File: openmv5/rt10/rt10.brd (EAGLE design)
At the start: 35.6 x 44.5 mm, 220 parts, among them CN1 S2B-PH-K-S(LF)(SN), IC1 LM66200DRLR, IC2 AP61300Z6-7, IC3 IS42S16160G-6BL, IC4 ATECC608B-MAHDA-T, IC5 IS25LP064D-JKLE-TR, IC6 IS25LP128F-JKLE-TR, IC7 MXC4005XC, IC8 MIMXRT1052DVL6B, IC9 KSZ8081RNDCA-TR, J1 USB4105-GF-A, J2 DNP, J3 DNP, J4 DF12-36-DS, J5 USD-1040310811, J6 DNP, J7 DNP, J8 3221-10-0300-00, M1 9774030151R, M2 9774030151R, Q1 2N7002KW_R1_00001, Q2 2N7002KW_R1_00001, Q3 2N7002KW_R1_00001, Q4 2N7002KW_R1_00001, Q5 2N7002KW_R1_00001, U1 MIC5365-3.3YMT-TZ, U2 BQ24075RGTR, U3 LBEE5KL1DX-883, Y1 SC32S-7PF20PPM, Y2 XRCGB24M000F3M00R0

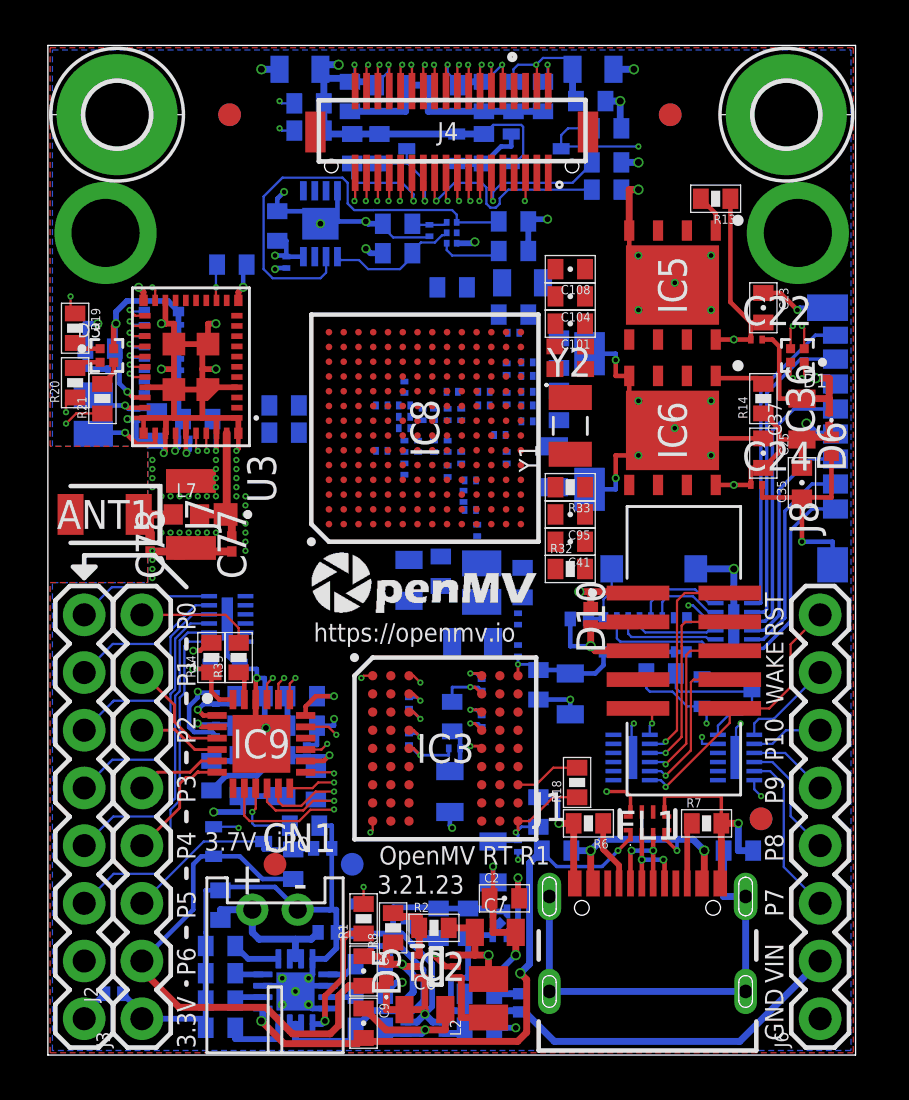
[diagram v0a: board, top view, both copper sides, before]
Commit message: Fix reverse protection on VIN, add TVS on FSIN, and fix USB current limits
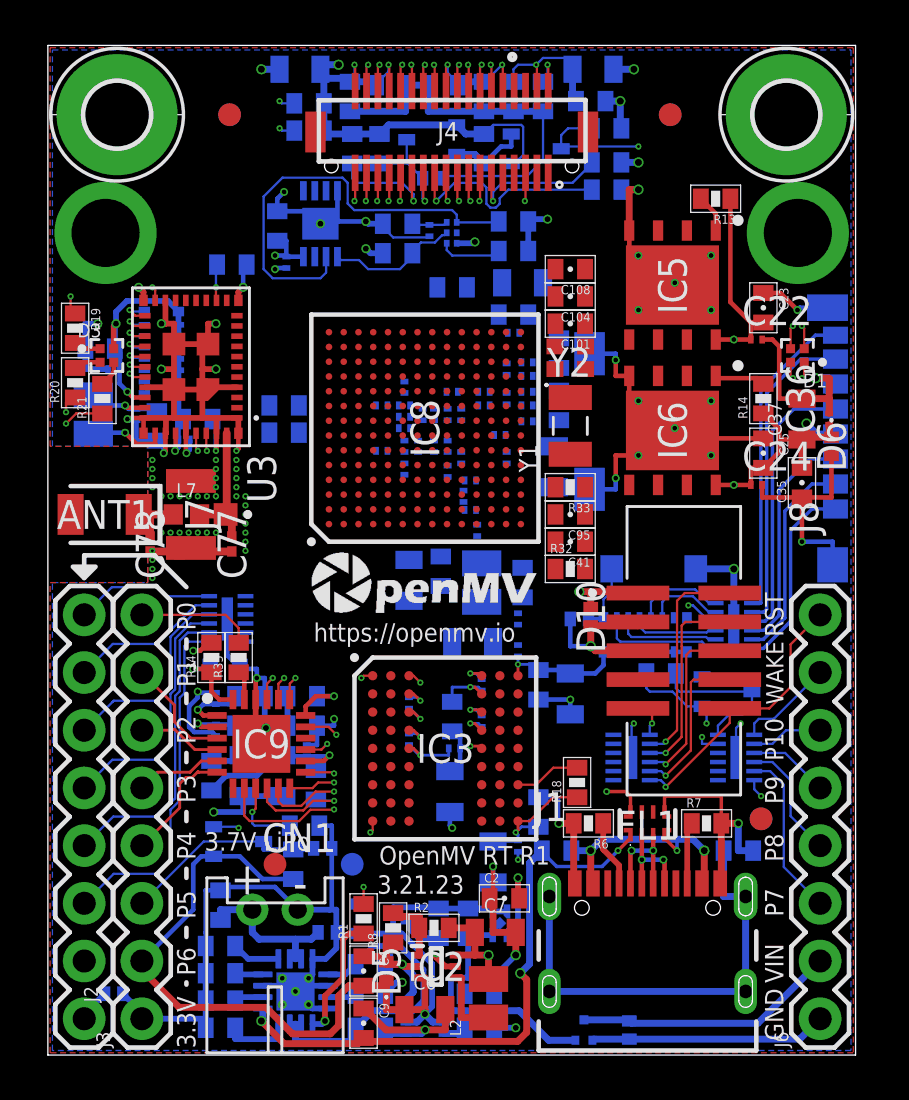
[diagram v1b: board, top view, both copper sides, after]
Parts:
- added D11: CPDQT5V0HE-HF, CPDQT5V0HE-HF:CPDQT5V0HEHF
- added Q6: PMXB120EPEZ, PMXB120EPEZ:PMXB120EPEZ
- R10: value 1.18K -> 3.3K
- R12: value 1.13K -> 8.2K
- moved D7 4.95 mm to (25.6, 1.10), turned to 270 degrees
- moved Q5 0.40 mm to (16.9, 40.3)
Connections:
- new net VIN_INT: C5.2, IC1.6, Q6.2
- net DCMI_FSIN: now also D11.1
- net GND: now also D11.2, Q6.1
- net VIN: now also Q6.3; no longer C5.2, IC1.6
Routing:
- net GND: track 237.6 -> 253.8 mm
- net VIN: track 19.4 -> 11.6 mm
- net VIN_INT: track 0.00 -> 6.33 mm

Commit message: Final
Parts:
- removed D11: CPDQT5V0HE-HF, CPDQT5V0HE-HF:CPDQT5V0HEHF
- removed L3: 100, sfe:C0402
- added C110: 1nF, sfe:0402-CAP
- added R41: 1M, sfe:0402-RES
- moved FD2 0.30 mm to (31.7, 10.4)
- moved FD4 0.30 mm to (31.7, 10.4)
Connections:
- net DCMI_FSIN: no longer D11.1
- net GND: now also C110.1, R41.2; no longer D11.2, L3.1
- net SHELL_GND: now also C110.2, R41.1; no longer L3.2
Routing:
- net GND: track 253.8 -> 248.6 mm, vias 102 -> 101
- net SHELL_GND: track 20.0 -> 21.6 mm
- net DCMI_FSIN: track 5.55 -> 4.33 mm

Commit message: Fix issues with part selection
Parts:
- L1: device sfe:C0402 -> SparkFun-Coils:0603
- moved C31 0.54 mm to (20.2, 9.40)
- moved C29 0.50 mm to (19.1, 8.50)
- moved C59 0.30 mm to (20.5, 31.5)
- moved C60 0.20 mm to (20.5, 32.4)
- moved C30 0.20 mm to (21.6, 10.9)
- moved L1 0.20 mm to (22.2, 9.00)
- moved C17 0.10 mm to (21.5, 16.3)
- moved C61 0.10 mm to (20.9, 33.9)
- moved C58 0.10 mm to (15.8, 20.9)
- moved R23 0.10 mm to (10.8, 8.30)
- moved R21 0.10 mm to (2.40, 28.8)
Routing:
- net GND: track 248.6 -> 250.2 mm, vias 101 -> 100
